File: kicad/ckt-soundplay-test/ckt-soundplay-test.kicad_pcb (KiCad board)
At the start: 2 copper layers, 106.7 x 73.7 mm, 26 parts, among them J1 Screw_Terminal_01x02, J2 Screw_Terminal_01x02, J3 Screw_Terminal_01x02, J4 Screw_Terminal_01x02, J8 Screw_Terminal_01x02, J9 Conn_01x05, SW1 FSM4JSMATR, SW2 FSM4JSMATR, SW3 FSM4JSMATR, SW4 FSM4JSMATR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

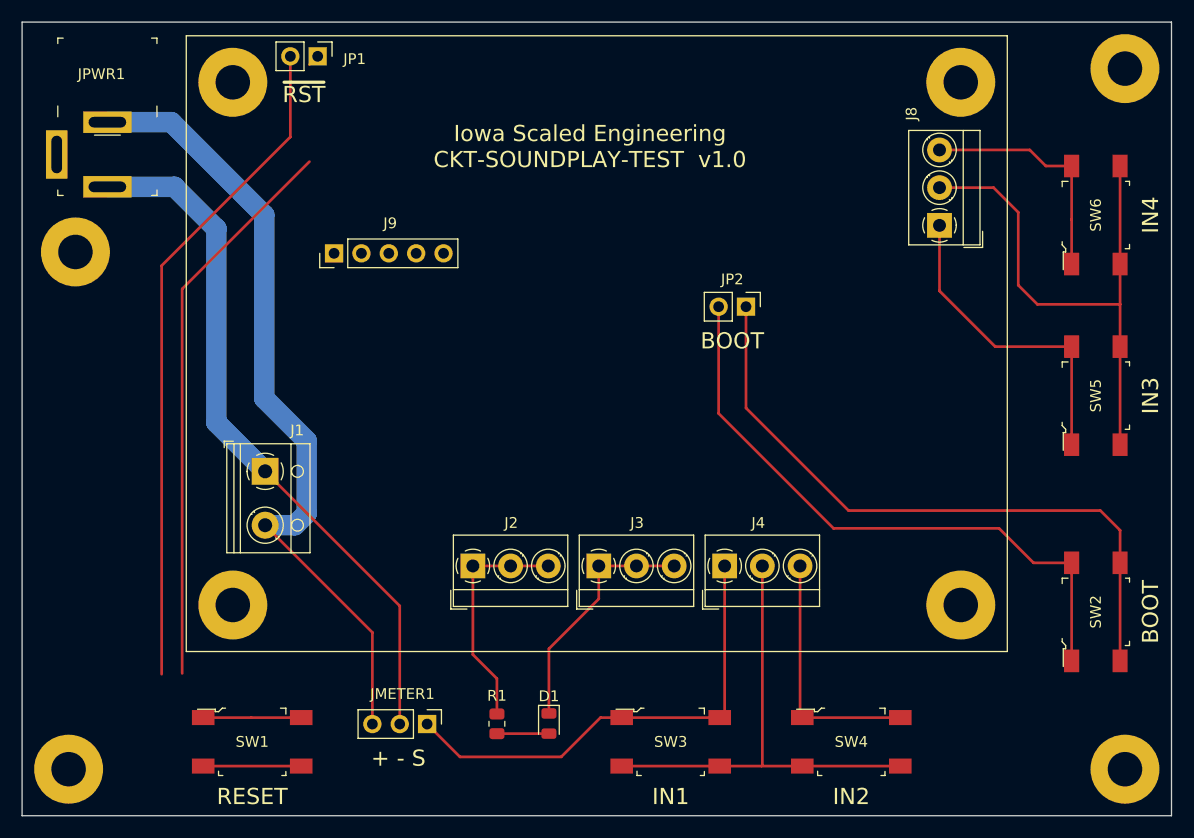
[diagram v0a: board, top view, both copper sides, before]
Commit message: Updated component locations and finished routing
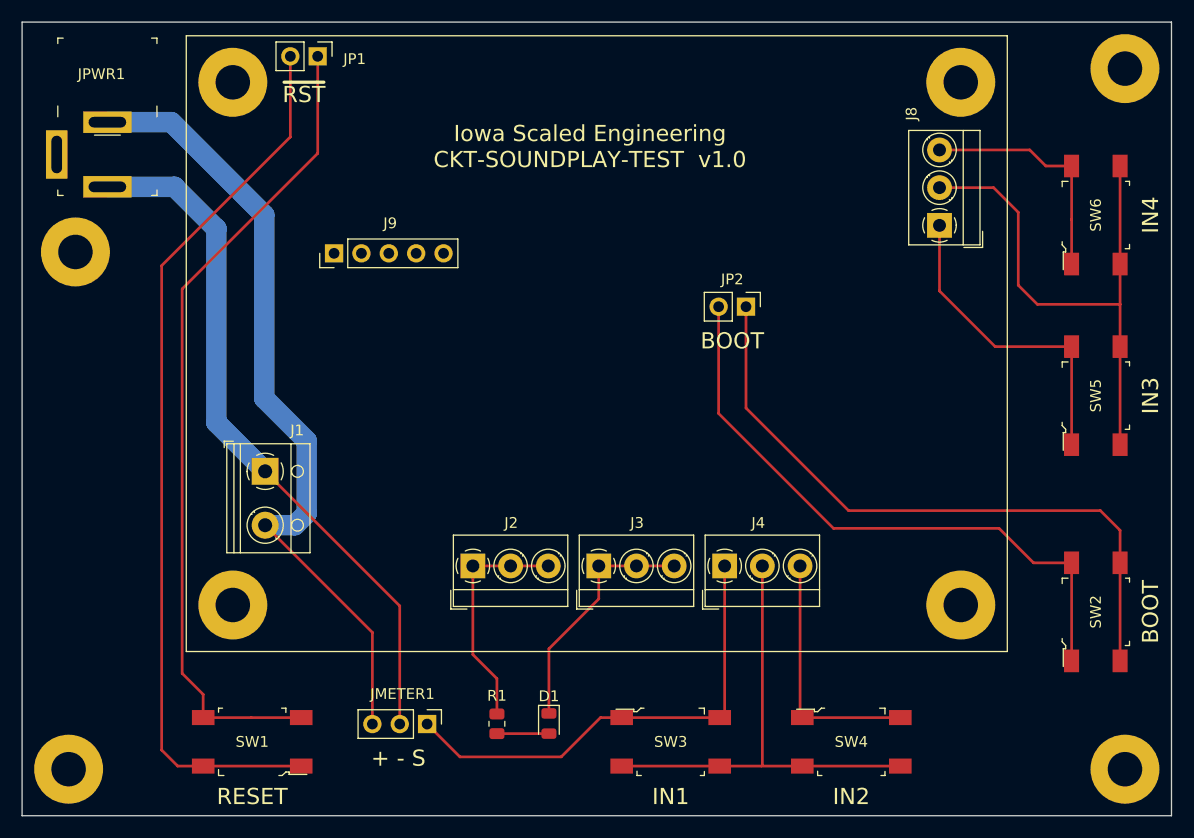
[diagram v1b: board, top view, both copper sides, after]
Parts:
- turned SW1 to 180 degrees
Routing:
- net Net-(JP1-Pad1): track 62.6 -> 76.5 mm
- net Net-(JP1-Pad2): track 71.4 -> 82.9 mm
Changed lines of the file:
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@@
   )
   (footprint "digikey-footprints:Switch_Tactile_SMD_6x6mm" (layer "F.Cu")
-    (at 107.718 109.982)
+    (at 107.718 109.982 180)
     (property "Category" "Switches")
     (property "DK_Datasheet_Link" "https://www.te.com/commerce/DocumentDelivery/DDEController?Action=srchrtrv&DocNm=2-1437565-7&DocType=Customer+Drawing&DocLang=English")
@@
     (fp_line (start -3 -2.725) (end -3 3) (layer "F.Fab") (width 0.1))
     (fp_line (start -2.7 -3) (end -3 -2.725) (layer "F.Fab") (width 0.1))
-    (pad "1" smd rect locked (at -4.55 -2.25 270) (size 1.4 2.1) (layers "F.Cu" "F.Paste" "F.Mask")
+    (pad "1" smd rect locked (at -4.55 -2.25 90) (size 1.4 2.1) (layers "F.Cu" "F.Paste" "F.Mask")
       (net 10 "Net-(JP1-Pad2)") (pintype "passive"))
-    (pad "2" smd rect locked (at 4.55 -2.25 270) (size 1.4 2.1) (layers "F.Cu" "F.Paste" "F.Mask")
+    (pad "2" smd rect locked (at 4.55 -2.25 90) (size 1.4 2.1) (layers "F.Cu" "F.Paste" "F.Mask")
       (net 10 "Net-(JP1-Pad2)") (pintype "passive"))
-    (pad "3" smd rect locked (at -4.55 2.25 270) (size 1.4 2.1) (layers "F.Cu" "F.Paste" "F.Mask")
+    (pad "3" smd rect locked (at -4.55 2.25 90) (size 1.4 2.1) (layers "F.Cu" "F.Paste" "F.Mask")
       (net 9 "Net-(JP1-Pad1)") (pintype "passive"))
-    (pad "4" smd rect locked (at 4.55 2.25 270) (size 1.4 2.1) (layers "F.Cu" "F.Paste" "F.Mask")
+    (pad "4" smd rect locked (at 4.55 2.25 90) (size 1.4 2.1) (layers "F.Cu" "F.Paste" "F.Mask")
       (net 9 "Net-(JP1-Pad1)") (pintype "passive"))
   )
@@
   (segment (start 180.594 69.378) (end 188.269 69.378) (width 0.254) (layer "F.Cu") (net 8))
   (segment (start 171.508 58.547) (end 176.53 58.547) (width 0.254) (layer "F.Cu") (net 8))
-  (segment (start 112.268 112.232) (end 103.168 112.232) (width 0.254) (layer "F.Cu") (net 9))
-  (segment (start 113.03 56.134) (end 101.219 67.945) (width 0.254) (layer "F.Cu") (net 9))
-  (segment (start 101.219 67.945) (end 101.219 103.632) (width 0.254) (layer "F.Cu") (net 9))
-  (segment (start 113.797 46.355) (end 113.03 47.122) (width 0.254) (layer "F.Cu") (net 9))
+  (segment (start 101.219 103.632) (end 101.219 67.945) (width 0.254) (layer "F.Cu") (net 9))
+  (segment (start 112.268 107.732) (end 107.627 107.732) (width 0.254) (layer "F.Cu") (net 9))
+  (segment (start 103.168 105.581) (end 103.168 107.732) (width 0.254) (layer "F.Cu") (net 9))
+  (segment (start 113.797 55.367) (end 113.797 46.355) (width 0.254) (layer "F.Cu") (net 9))
+  (segment (start 101.219 67.945) (end 113.797 55.367) (width 0.254) (layer "F.Cu") (net 9))
+  (segment (start 107.627 107.732) (end 103.168 107.732) (width 0.254) (layer "F.Cu") (net 9))
+  (segment (start 101.219 103.632) (end 103.168 105.581) (width 0.254) (layer "F.Cu") (net 9))
+  (segment (start 112.268 112.232) (end 103.168 112.232) (width 0.254) (layer "F.Cu") (net 10))
+  (segment (start 99.314 110.744) (end 100.802 112.232) (width 0.254) (layer "F.Cu") (net 10))
+  (segment (start 99.314 65.786) (end 99.314 110.744) (width 0.254) (layer "F.Cu") (net 10))
+  (segment (start 111.257 46.355) (end 111.257 53.843) (width 0.254) (layer "F.Cu") (net 10))
   (segment (start 111.257 53.843) (end 99.314 65.786) (width 0.254) (layer "F.Cu") (net 10))
-  (segment (start 111.257 46.355) (end 111.257 53.843) (width 0.254) (layer "F.Cu") (net 10))
-  (segment (start 99.314 65.786) (end 99.314 103.704) (width 0.254) (layer "F.Cu") (net 10))
-  (segment (start 112.268 107.732) (end 107.627 107.732) (width 0.254) (layer "F.Cu") (net 10))
-  (segment (start 107.627 107.732) (end 103.168 107.732) (width 0.254) (layer "F.Cu") (net 10))
+  (segment (start 100.802 112.232) (end 103.168 112.232) (width 0.254) (layer "F.Cu") (net 10))
   (segment (start 153.548 69.596) (end 153.548 78.999) (width 0.254) (layer "F.Cu") (net 11))
   (segment (start 188.269 102.467) (end 188.269 93.367) (width 0.254) (layer "F.Cu") (net 11))
@@
   (segment (start 171.508 62.047) (end 171.508 68.13) (width 0.254) (layer "F.Cu") (net 24))
   (segment (start 183.769 61.504) (end 183.769 65.637) (width 0.254) (layer "F.Cu") (net 25))
-  (segment (start 183.749 61.524) (end 183.769 61.504) (width 0.254) (layer "F.Cu") (net 25))
   (segment (start 179.888 55.047) (end 181.378 56.537) (width 0.254) (layer "F.Cu") (net 25))
   (segment (start 171.508 55.047) (end 179.888 55.047) (width 0.254) (layer "F.Cu") (net 25))

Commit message: Added holes for test points and rewired slightly
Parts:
- added TP1: TestPoint, Connector_PinHeader_2.54mm:PinHeader_1x01_P2.54mm_Vertical, F.Cu at (151.4, 97.5)
- added TP2: TestPoint, Connector_PinHeader_2.54mm:PinHeader_1x01_P2.54mm_Vertical, F.Cu at (158.6, 97.5)
- added TP3: TestPoint, Connector_PinHeader_2.54mm:PinHeader_1x01_P2.54mm_Vertical, F.Cu at (175.4, 62.1)
- added TP4: TestPoint, Connector_PinHeader_2.54mm:PinHeader_1x01_P2.54mm_Vertical, F.Cu at (175.4, 55.0)
- added TP5: TestPoint, Connector_PinHeader_2.54mm:PinHeader_1x01_P2.54mm_Vertical, F.Cu at (105.2, 84.8)
- added TP6: TestPoint, Connector_PinHeader_2.54mm:PinHeader_1x01_P2.54mm_Vertical, F.Cu at (105.2, 89.9)
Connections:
- J4 pad 2: Net-(J4-Pad2) -> GND
- J8 pad 2: Net-(J8-Pad2) -> GND
- JP1 pad 2: Net-(JP1-Pad2) -> GND
- JP2 pad 1: Net-(JP2-Pad1) -> GND
- SW1 pad 1: Net-(JP1-Pad2) -> GND
- SW1 pad 2: Net-(JP1-Pad2) -> GND
- SW2 pad 3: Net-(JP2-Pad1) -> GND
- SW2 pad 4: Net-(JP2-Pad1) -> GND
- SW3 pad 3: Net-(J4-Pad2) -> GND
- SW3 pad 4: Net-(J4-Pad2) -> GND
- SW4 pad 3: Net-(J4-Pad2) -> GND
- SW4 pad 4: Net-(J4-Pad2) -> GND
- SW5 pad 3: Net-(J8-Pad2) -> GND
- SW5 pad 4: Net-(J8-Pad2) -> GND
- SW6 pad 3: Net-(J8-Pad2) -> GND
- SW6 pad 4: Net-(J8-Pad2) -> GND
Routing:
- net GND: track 74.3 -> 385.3 mm
- net Net-(JP1-Pad2): track 82.9 -> 0.00 mm
- net Net-(JP2-Pad1): track 60.9 -> 0.00 mm
- net Net-(J8-Pad2): track 51.1 -> 0.00 mm
- net Net-(J4-Pad2): track 44.3 -> 0.00 mm
- net Net-(J8-Pad1): track 29.6 -> 33.5 mm
- net /VPWR: track 64.8 -> 68.5 mm
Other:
- board text added: "- + S"
- board text removed: "+ - S"

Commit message: Bumped rev to 1.2
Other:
- board text added: "Iowa Scaled Engineering CKT-SOUNDPLAY-TEST v1.2"
- board text removed: "Iowa Scaled Engineering CKT-SOUNDPLAY-TEST v1.0"
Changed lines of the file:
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@@
     (effects (font (size 1.5 1.5) (thickness 0.3)))
   )
-  (gr_text "Iowa Scaled Engineering\nCKT-SOUNDPLAY-TEST  v1.0\n" (at 139.065 54.737) (layer "F.SilkS")
+  (gr_text "Iowa Scaled Engineering\nCKT-SOUNDPLAY-TEST  v1.2\n" (at 139.065 54.737) (layer "F.SilkS")
     (effects (font (size 1.5 1.5) (thickness 0.3)))
   )
